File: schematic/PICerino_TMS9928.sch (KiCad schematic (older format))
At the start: 61 parts, among them CON1 PICERINO-EDGE, J1 Conn_01x02, J10 Conn_01x08, J11 Conn_01x08, J12 Conn_01x03, J2 Y_Conn_01x02, J3 BY_Conn_01x02, J4 RY_Conn_01x02, J7 Conn_01x02, J8 Conn_01x02, J9 Conn_01x02, Y1 Crystal

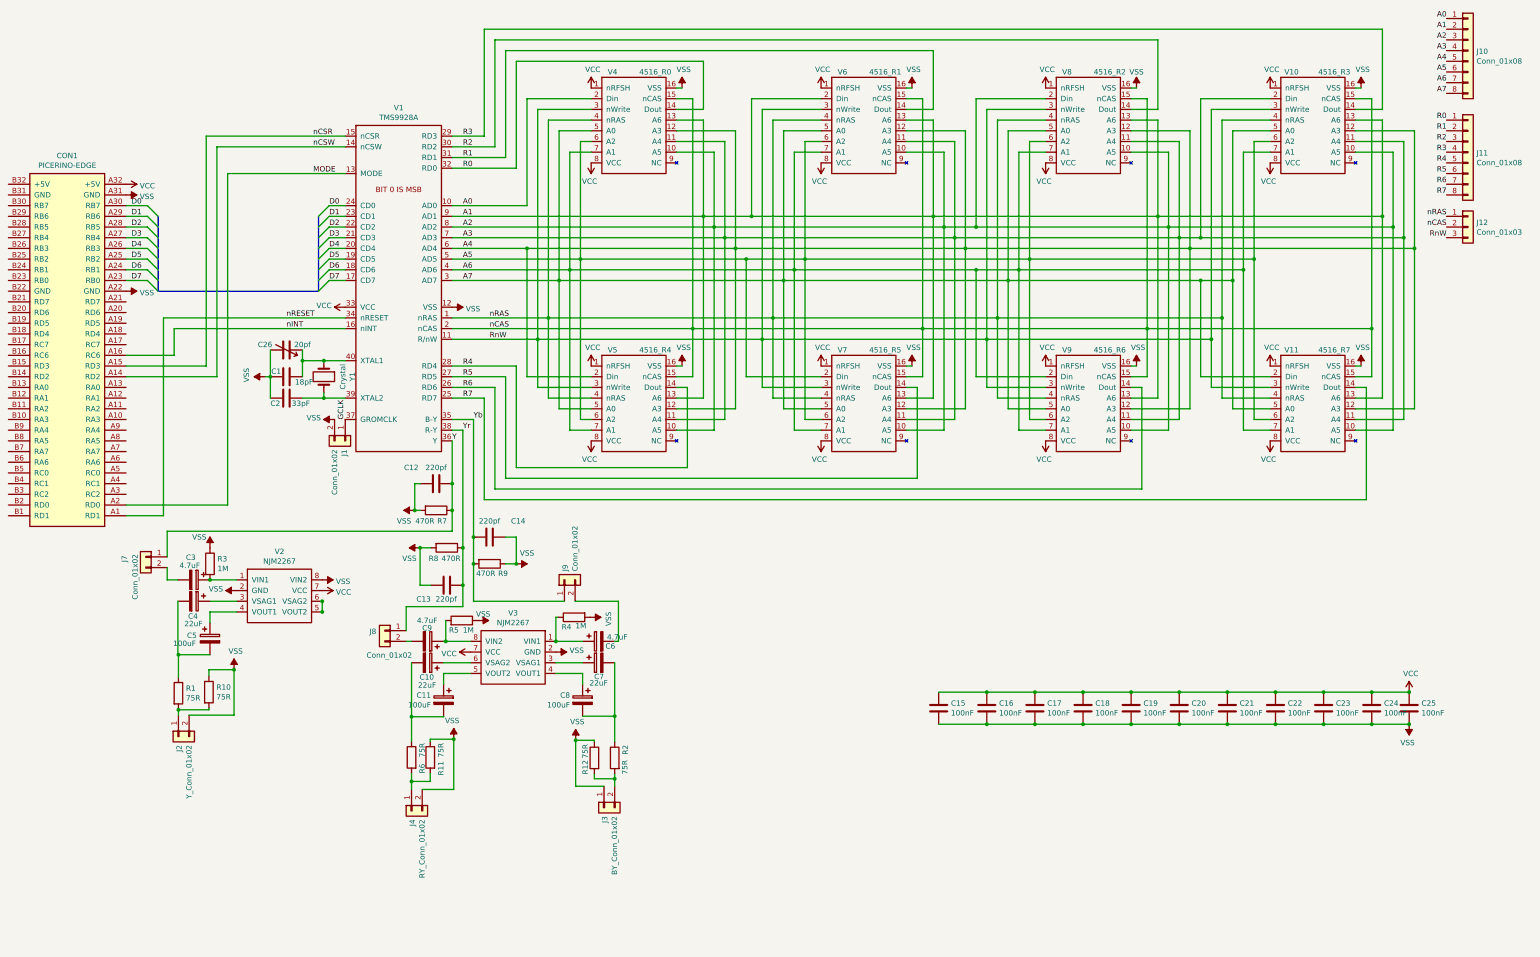
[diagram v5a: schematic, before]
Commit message: schematic cleanup in progress. changed address/write data lines to bus. cleaned up some component stuffs.
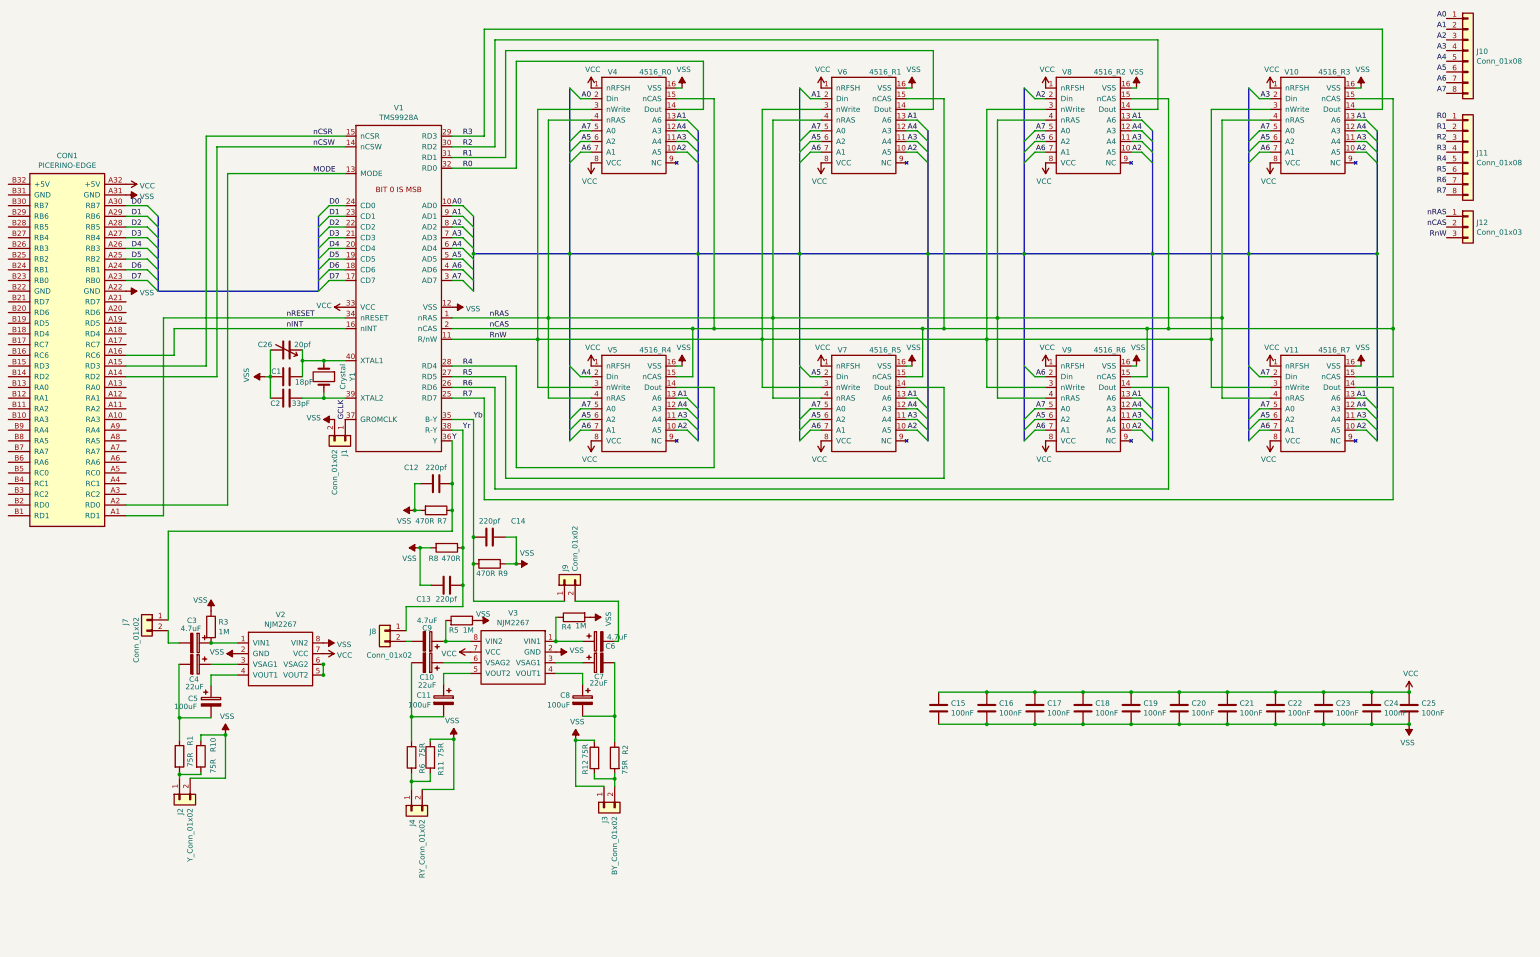
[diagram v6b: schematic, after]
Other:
- moved on the sheet: C3, C4, C5, J2, J7, R1, R10, R3, V2

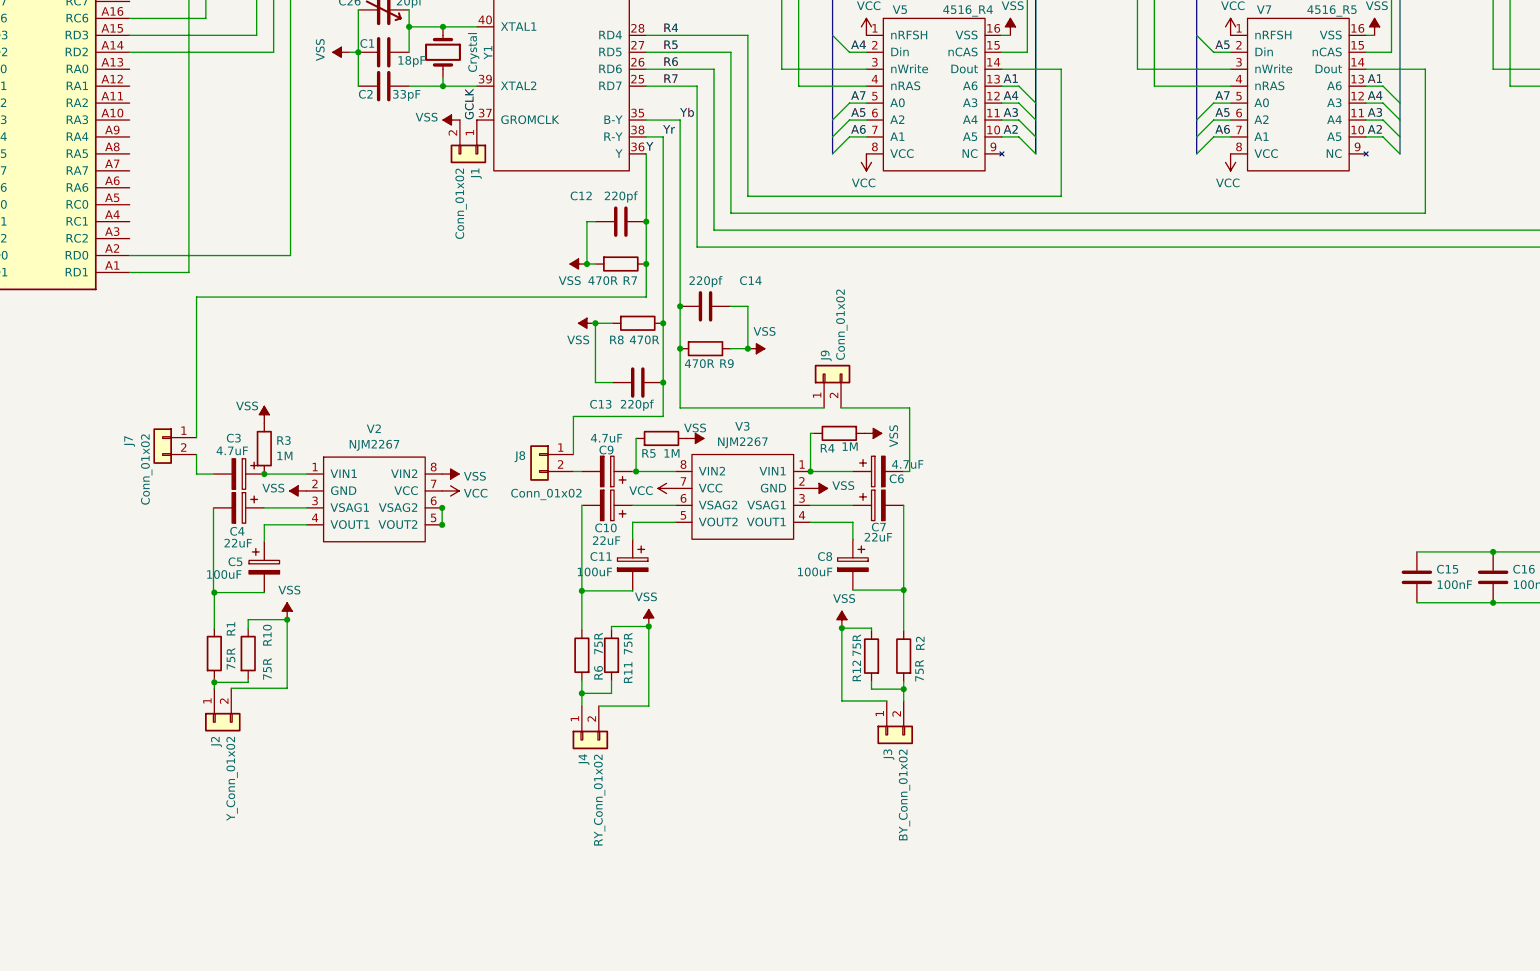
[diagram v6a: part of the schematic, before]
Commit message: major change to video section. dark green seemed off. tested adg453 sending output to gnd on that negative sync pulse. worked well. using mostly ti's idea with a modern sync strip ic. decided to use the other left over video opamp for a dc output. not tested at all but will be interesting since Y is supposed to be dc offset (works as ac offset though...whatever). This is intended to be a adjustable and usable for both the 9918 and 9928.
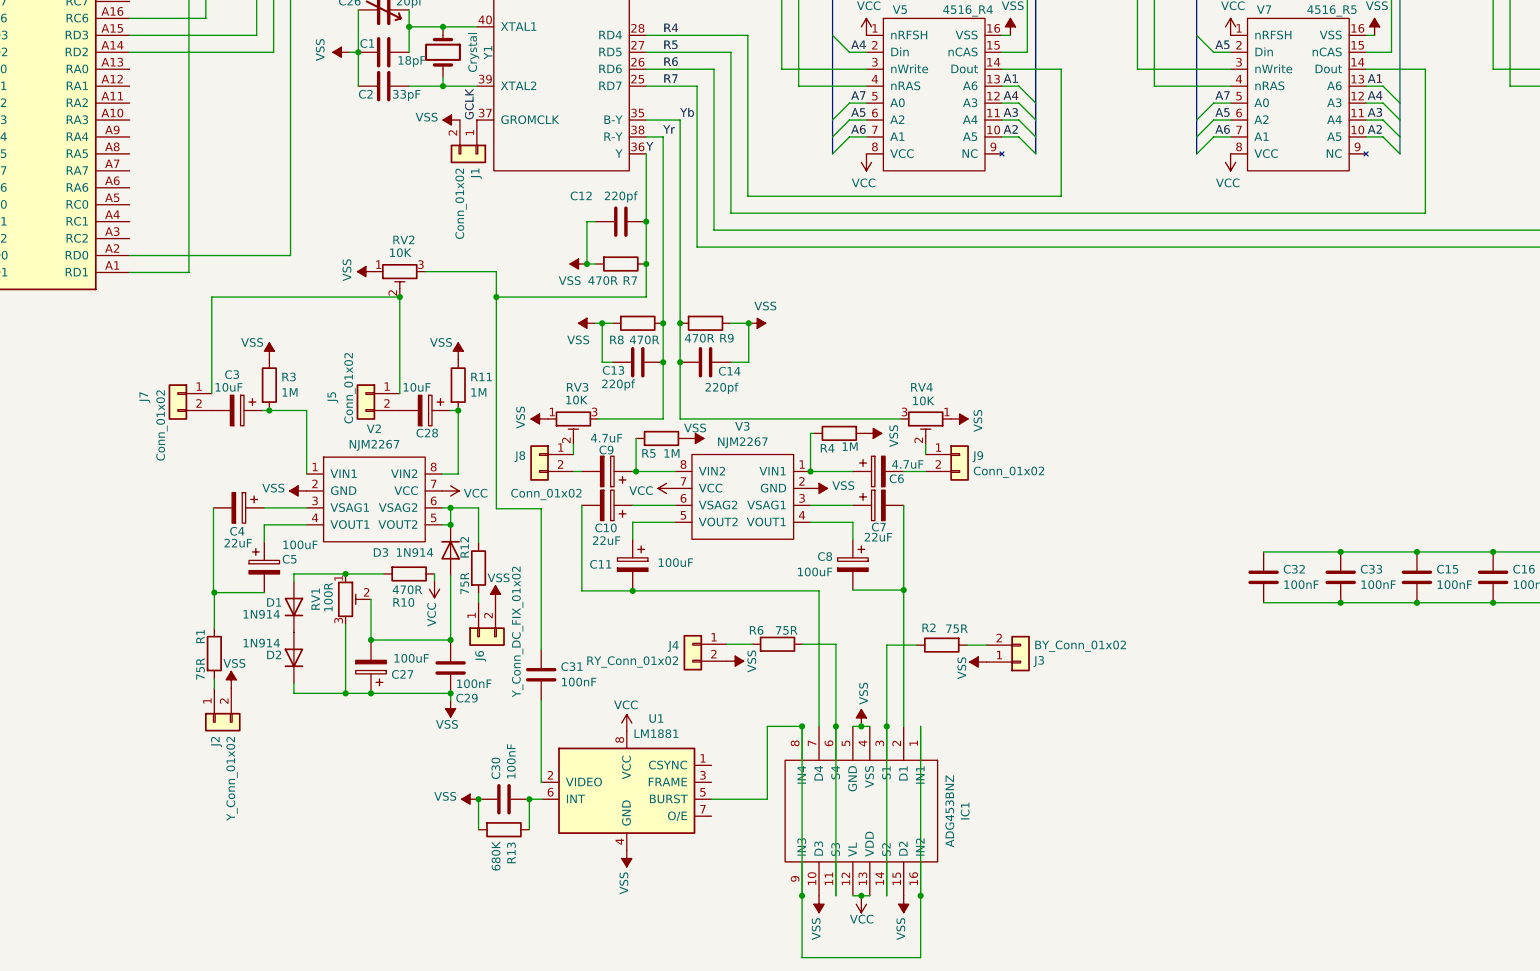
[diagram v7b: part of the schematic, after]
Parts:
- added C27: 100uF, Capacitor_THT:CP_Radial_D7.5mm_P2.50mm, symbol Device:CP
- added C28: 10uF, Capacitor_THT:CP_Radial_D5.0mm_P2.00mm, symbol Device:CP
- added C29, C30, C31, C32, C33: 100nF, Capacitor_THT:C_Disc_D4.7mm_W2.5mm_P5.00mm, symbol Device:C
- added D1, D2, D3: 1N914, Diode_THT:D_DO-35_SOD27_P7.62mm_Horizontal, symbol Diode:1N914
- added IC1: ADG453BNZ, Package_SO:SOIC-16_3.9x9.9mm_P1.27mm, symbol ADG453BNZ:ADG453BNZ
- added J5: Conn_01x02, Connector_PinHeader_2.54mm:PinHeader_1x02_P2.54mm_Vertical, symbol Connector_Generic:Conn_01x02
- added J6: Y_Conn_DC_FIX_01x02, Connector_PinHeader_2.54mm:PinHeader_1x02_P2.54mm_Vertical, symbol Connector_Generic:Conn_01x02
- added R13: 680K, Resistor_THT:R_Axial_DIN0207_L6.3mm_D2.5mm_P7.62mm_Horizontal, symbol Device:R
- added RV1: 100R, Potentiometer_THT:Potentiometer_Piher_PT-6-V_Vertical_Hole, symbol Device:R_POT_TRIM
- added RV2, RV3, RV4: 10K, Potentiometer_THT:Potentiometer_Piher_PT-6-V_Vertical_Hole, symbol Device:R_POT_TRIM
- added U1: LM1881, Package_DIP:DIP-8_W7.62mm_LongPads, symbol Video:LM1881
- C3: value 4.7uF -> 10uF
- R10: value 75R -> 470R; footprint Resistor_THT:R_Axial_DIN0207_L6.3mm_D2.5mm_P2.54mm_Vertical -> Resistor_THT:R_Axial_DIN0207_L6.3mm_D2.5mm_P7.62mm_Horizontal
- R11: value 75R -> 1M; footprint Resistor_THT:R_Axial_DIN0207_L6.3mm_D2.5mm_P2.54mm_Vertical -> Resistor_THT:R_Axial_DIN0207_L6.3mm_D2.5mm_P7.62mm_Horizontal
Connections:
- net VCC: now also R10.1, C32.1, C33.1, IC1.12 (VL), IC1.13 (VDD), U1.8 (VCC)
- net VSS: now also C27.1, C29.1, C30.1, C32.2, C33.2, D2.1 (K), IC1.10 (D3), IC1.15 (D2), IC1.4 (VSS), IC1.5 (GND), J6.2 (Pin_2), R13.2, RV1.3, RV2.1, RV3.1, RV4.1, U1.4 (GND); no longer R10.1, R12.1, V2.8 (VIN2)
- net Y: now also C31.1, RV2.3; no longer J7.1 (Pin_1)
- net Yb: now also RV4.3; no longer J9.1 (Pin_1)
- net Yr: now also RV3.3; no longer J8.1 (Pin_1)
- net at V2.5 (VOUT2), V2.6 (VSAG2): now also R12.1, D3.1 (K)
- net at J2.1 (Pin_1), R1.2: no longer R10.2
- net at J4.1 (Pin_1), R6.2: no longer R11.2
- net at J3.2 (Pin_2), R2.2: no longer R12.2
- net at C7.2, C8.2: now also IC1.2 (D1); no longer R2.1
- net at C10.2, C11.2: now also IC1.7 (D4); no longer R6.1
- new net: C28.1, R11.2, V2.8 (VIN2)
- new net: J9.1 (Pin_1), RV4.2
- new net: J8.1 (Pin_1), RV3.2
- new net: J5.1 (Pin_1), J7.1 (Pin_1), RV2.2
- new net: C31.2, U1.2 (VIDEO)
- new net: IC1.1 (IN1), IC1.16 (IN2), IC1.8 (IN4), IC1.9 (IN3), U1.5 (BURST)
- new net: C30.2, R13.1, U1.6 (INT)
- new net: IC1.11 (S3), IC1.6 (S4), R6.1
- new net: IC1.14 (S2), IC1.3 (S1), R2.1
- new net: C28.2, J5.2 (Pin_2)
- new net: J6.1 (Pin_1), R12.2
- new net: C27.2, C29.2, D3.2 (A), RV1.2
- new net: D1.1 (K), D2.2 (A)
- new net: D1.2 (A), R10.2, RV1.1
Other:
- moved on the sheet: C13, C14, C3, J3, J4, J7, J9, R2, R3, R6, R9
